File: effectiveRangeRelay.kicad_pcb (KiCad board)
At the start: 8 copper layers, 50 x 80 mm, 45 parts, among them J2 OUT, J3 EXT_BUS, J4 OUT, J6 VBUS_EXT, J7 MRHAT_CTRL, K1 J107F1CS125VDC.36, Q1 GSFF3134, Q2 GSFF3134, U2 LMS3635LQURNLRQ1, U3 MCP3425A0T-E/CH

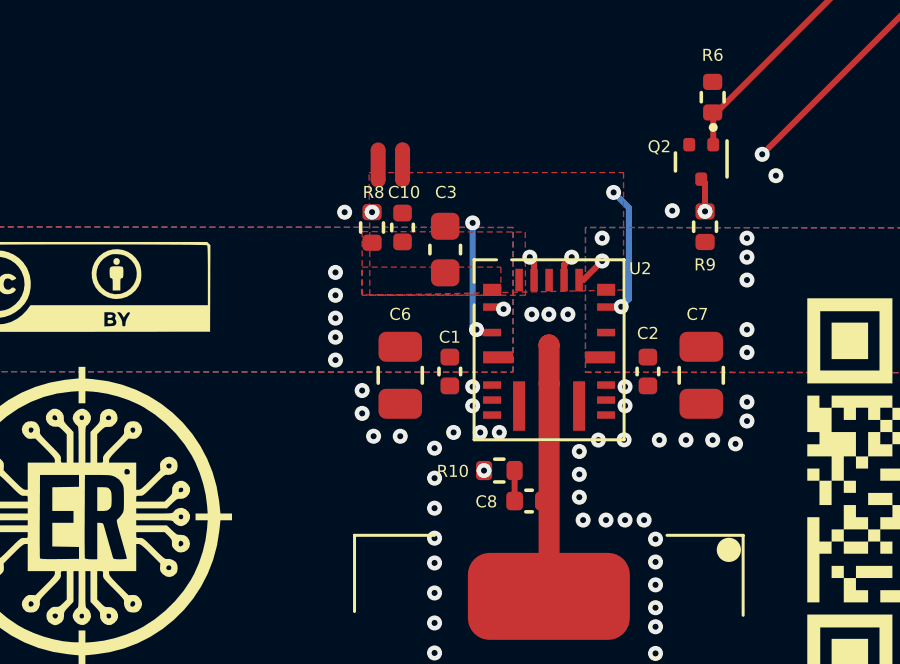
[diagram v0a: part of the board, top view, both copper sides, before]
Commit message: fix erc errors
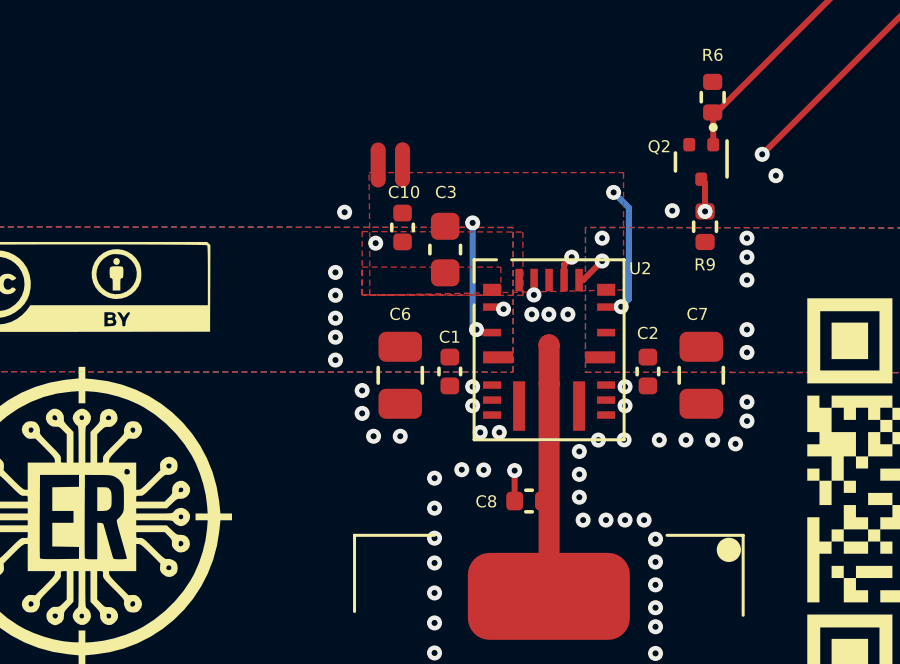
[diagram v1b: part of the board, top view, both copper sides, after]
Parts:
- removed R10, R8: 2, Resistor_SMD:R_0402_1005Metric
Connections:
- C10 pad 1: /power/BIAS -> +5VP
- C8 pad 1: /power/CBOOT_LIM -> /power/CBOOT
- U2 pad 22: /power/BIAS -> +5VP
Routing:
- net /power/CBOOT_LIM: track 1.02 -> 0.00 mm
- net +5VP: track 65.1 -> 64.2 mm
- net /power/CBOOT: track 7.19 -> 7.78 mm
- removed copper zone on F.Cu, net /power/BIAS

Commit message: fix drc errors
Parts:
- moved NT2 1.06 mm to (122.8, 121.6)
- moved NT1 0.23 mm to (121.1, 121.6)
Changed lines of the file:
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@@
 	(footprint "NetTie:NetTie-2_SMD_Pad0.5mm"
 		(layer "F.Cu")
-		(at 121.7662 121.7266 -90)
+		(at 122.821 121.631 -90)
 		(descr "Net tie, 2 pin, 0.5mm square SMD pads")
 		(tags "net tie")
@@
 	(footprint "NetTie:NetTie-2_SMD_Pad0.5mm"
 		(layer "F.Cu")
-		(at 120.9534 121.7346 -90)
+		(at 121.131 121.591 -90)
 		(descr "Net tie, 2 pin, 0.5mm square SMD pads")
 		(tags "net tie")

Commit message: fix drc errors
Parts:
- moved NT2 0.87 mm to (122.0, 121.7)
- moved NT1 0.23 mm to (121.0, 121.7)
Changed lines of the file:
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@@
 	(footprint "NetTie:NetTie-2_SMD_Pad0.5mm"
 		(layer "F.Cu")
-		(at 122.821 121.631 -90)
+		(at 121.9534 121.7346 -90)
 		(descr "Net tie, 2 pin, 0.5mm square SMD pads")
 		(tags "net tie")
@@
 	(footprint "NetTie:NetTie-2_SMD_Pad0.5mm"
 		(layer "F.Cu")
-		(at 121.131 121.591 -90)
+		(at 120.9534 121.7346 -90)
 		(descr "Net tie, 2 pin, 0.5mm square SMD pads")
 		(tags "net tie")
